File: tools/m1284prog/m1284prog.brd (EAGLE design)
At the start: 69.5 x 30.5 mm, 10 parts, among them IC1 ATMEGA644-20PU, J1 AVR_SPI_PROG_3X2PTH

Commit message: Update several tool boards.
+ AEPRO had the wrong socket size; the ZIF footprint was for
  a narrow 28-pin DIP.
+ AEPRO was missing an inverter on the LEDs.
+ M328PGM had a serial line tied to RST: any attempt at using the
  UART caused the board to reset.
+ M1284PGM had no silkscreen markings to identify the board.
+ M1284PGM had no decoupling capacitor for the MCU.
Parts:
- added C1: 0.1uF, capacitor-wima:C2.5-3
- R1: value (none) -> 10K
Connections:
- net GND: now also C1.2
- net VCC: now also C1.1
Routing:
- net VCC: track 94.5 -> 0.00 mm
- net N$4: track 93.2 -> 0.00 mm
- net GND: track 93.0 -> 0.00 mm
- net N$6: track 49.1 -> 0.00 mm
- net N$5: track 44.1 -> 0.00 mm
- net N$3: track 42.5 -> 0.00 mm
- net N$12: track 29.4 -> 0.00 mm
- net N$13: track 25.9 -> 0.00 mm
- net N$7: track 23.6 -> 0.00 mm
- net N$11: track 18.3 -> 0.00 mm
- net N$8: track 18.3 -> 0.00 mm
- net N$1: track 6.19 -> 0.00 mm
- net N$2: track 5.15 -> 0.00 mm
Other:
- board text added: "16MHz"
- board text added: "330R"
- board text added: "ICSP"
- board text added: "K_ISOM/OAK_CA"
- board text added: "M1284PROG"
- board text added: "PA3"
- board text added: "RES"
- board text added: "RESET"
- board text added: "REV1/2019-09-30"
- board text added: "WNTRMUTE"

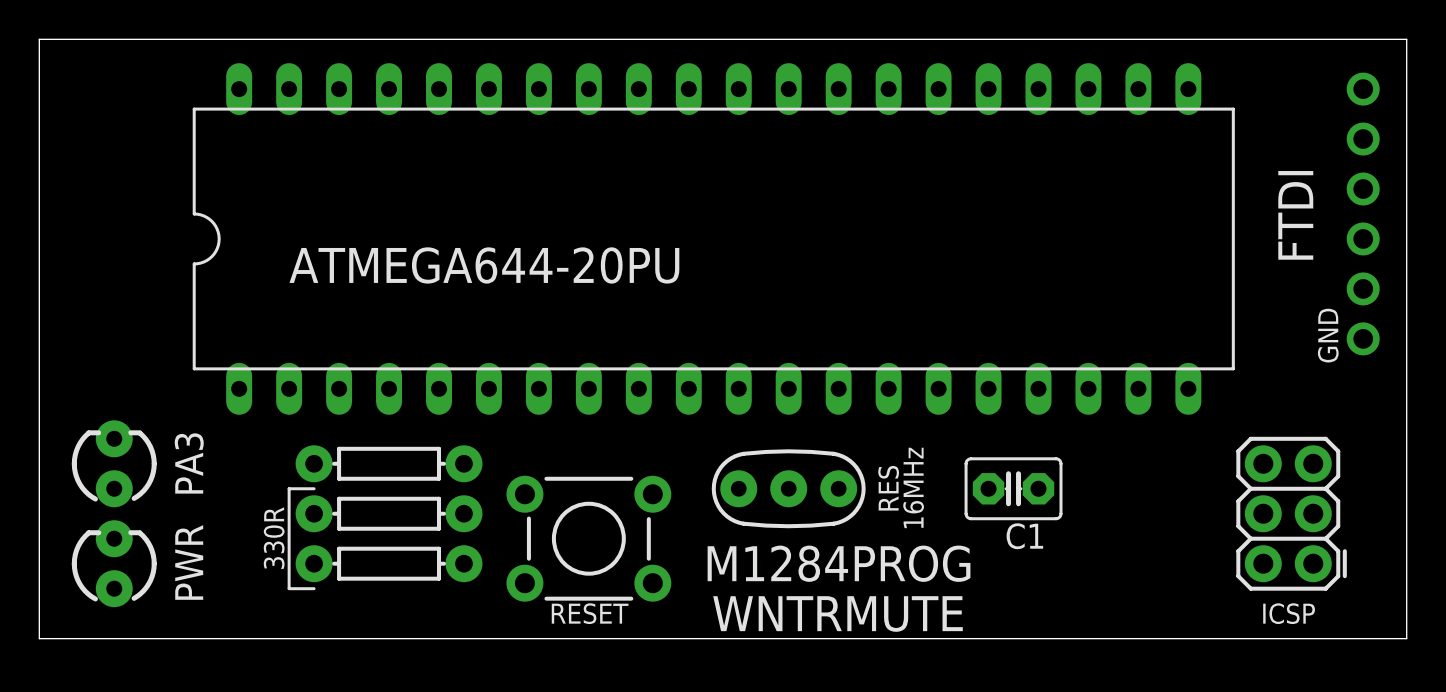
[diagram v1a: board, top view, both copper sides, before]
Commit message: Fix UART issues in programmers.
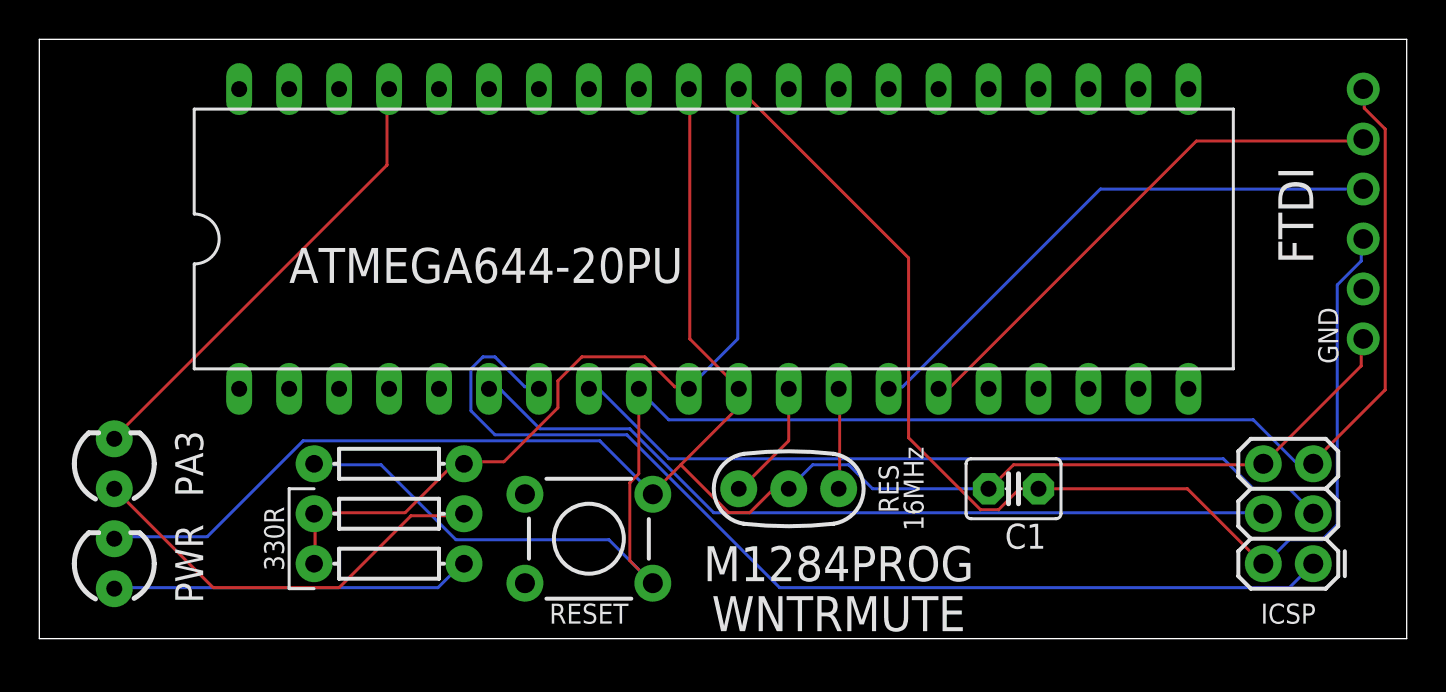
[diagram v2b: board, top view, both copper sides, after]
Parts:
- added FRAME1: FRAME-LETTER, SparkFun-Aesthetics:CREATIVE_COMMONS
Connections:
- removed net N$12: CN1.5, IC1.14
- removed net N$13: CN1.4, IC1.15
- new net N$10: CN1.5, IC1.15
- new net N$9: CN1.4, IC1.14
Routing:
- net VCC: track 0.00 -> 105.3 mm
- net GND: track 0.00 -> 95.3 mm
- net N$4: track 0.00 -> 87.3 mm
- net N$5: track 0.00 -> 53.6 mm
- net N$3: track 0.00 -> 42.0 mm
- net N$6: track 0.00 -> 39.5 mm
- net N$9: track 0.00 -> 28.3 mm
- net N$10: track 0.00 -> 26.9 mm
- net N$7: track 0.00 -> 23.6 mm
- net N$8: track 0.00 -> 21.4 mm
- net N$11: track 0.00 -> 18.3 mm
- net N$1: track 0.00 -> 6.19 mm
- net N$2: track 0.00 -> 5.15 mm
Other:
- board text added: "REV2/2019-10-02"
- board text removed: "REV1/2019-09-30"
